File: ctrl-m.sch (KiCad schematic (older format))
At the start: 32 parts, among them J1 USB_B, J10 Conn_01x04, J11 Conn_01x05, J12 Conn_01x04, J2 Conn_ARM_JTAG_SWD_10, J3 Conn_01x01, J4 Conn_01x01, J5 Conn_01x01, J6 Conn_01x01, J7 Conn_01x16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

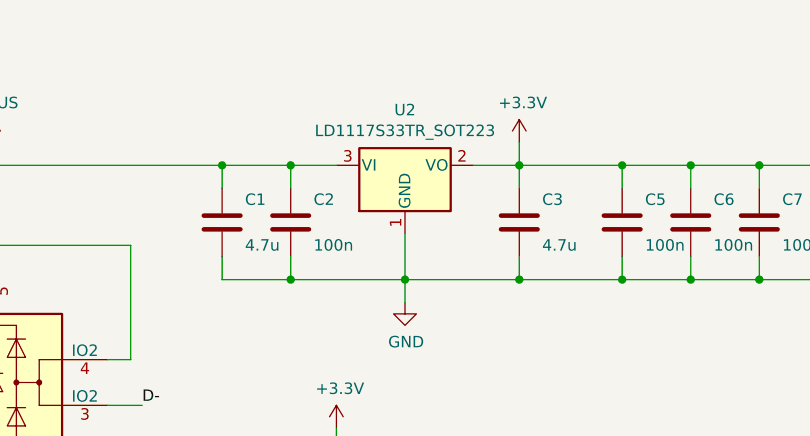
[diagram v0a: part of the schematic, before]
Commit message: Changed LDO type to one that is stable with ceramic capacitors
LD1117 is unstable with this low output capacitance and in general with
ceramic capacitors.

Also it needs 10 mA minimum load which is not guaranteed when all LEDs are off.

Replaced with a much more recent chip the XC6206P332PR
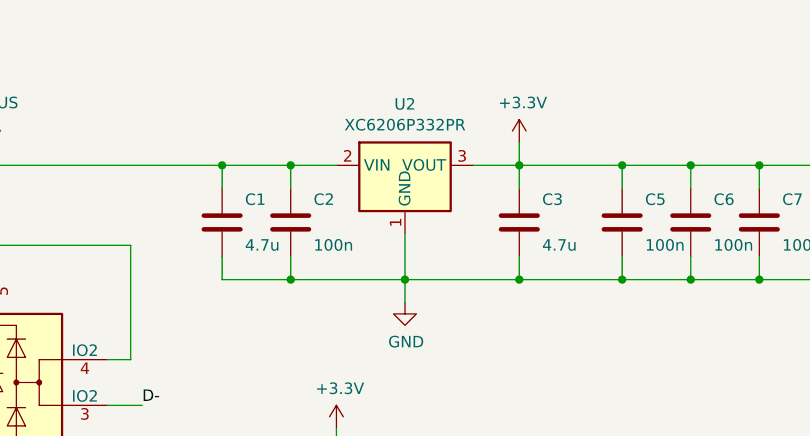
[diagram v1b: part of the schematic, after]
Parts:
- removed U2: LD1117S33TR_SOT223, Package_TO_SOT_SMD:SOT-223-3_TabPin2, symbol Regulator_Linear:LD1117S33TR_SOT223
- added U2: XC6206P332PR, Package_TO_SOT_SMD:SOT-89-3, symbol Regulator_Linear:HT75xx-1-SOT89
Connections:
- net +3V3: now also U2.3 (VOUT)
- net GND: now also U2.1 (GND)
- net VBUS: now also U2.2 (VIN)
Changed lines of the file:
@@
 Sheet 1 1
 Title "Model M Controller based on STM32F072"
-Date "2021-03-24"
+Date "2021-03-27"
 Rev "1.0"
 Comp "nuess0r"
@@
 F 3 "~" H 3500 1550 50  0001 C CNN
 	1    3500 1550
-	1    0    0    -1
-$EndComp
-$Comp
-L Regulator_Linear:LD1117S33TR_SOT223 U2
-U 1 1 5F72E7C7
-P 4300 1300
-F 0 "U2" H 4300 1542 50  0000 C CNN
-F 1 "LD1117S33TR_SOT223" H 4300 1451 50  0000 C CNN
-F 2 "Package_TO_SOT_SMD:SOT-223-3_TabPin2" H 4300 1500 50  0001 C CNN
-F 3 "http://www.st.com/st-web-ui/static/active/en/resource/technical/document/datasheet/CD00000544.pdf" H 4400 1050 50  0001 C CNN
-	1    4300 1300
 	1    0    0    -1
 $EndComp
@@
 Wire Bus Line
 	9400 850  9400 2500
+$Comp
+L Regulator_Linear:HT75xx-1-SOT89 U2
+U 1 1 606051D6
+P 4300 1400
+F 0 "U2" H 4300 1767 50  0000 C CNN
+F 1 "XC6206P332PR" H 4300 1676 50  0000 C CNN
+F 2 "Package_TO_SOT_SMD:SOT-89-3" H 4300 1725 50  0001 C CIN
+F 3 "https://www.torexsemi.com/file/xc6206/XC6206.pdf" H 4300 1500 50  0001 C CNN
+	1    4300 1400
+	1    0    0    -1
+$EndComp
 $EndSCHEMATC
